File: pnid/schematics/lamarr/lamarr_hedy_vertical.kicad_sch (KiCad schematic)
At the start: 102 parts, among them U1 Rocket_Big

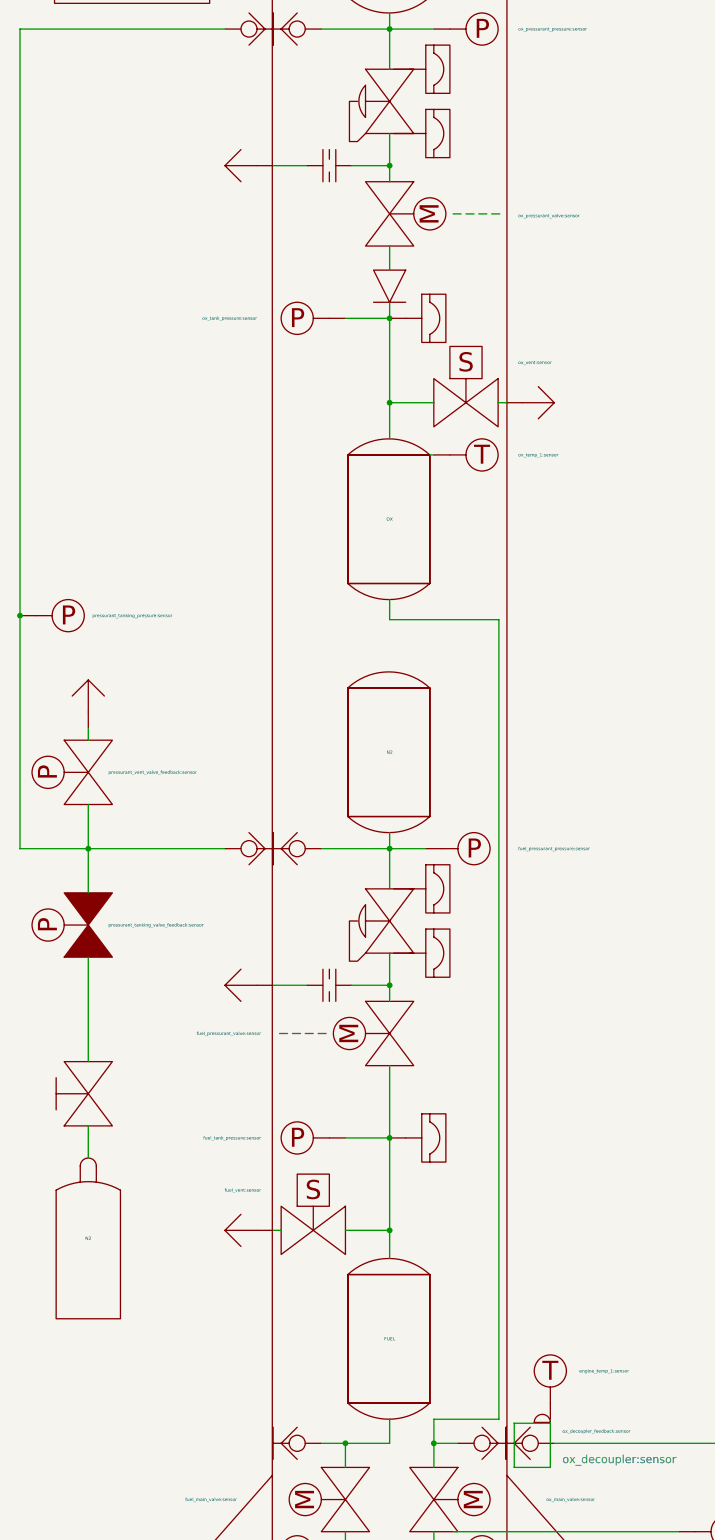
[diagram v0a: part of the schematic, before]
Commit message: Added fuel/ox pressurant vent to the pnid & mapping Added servo controlled throttle to the pnid & mapping
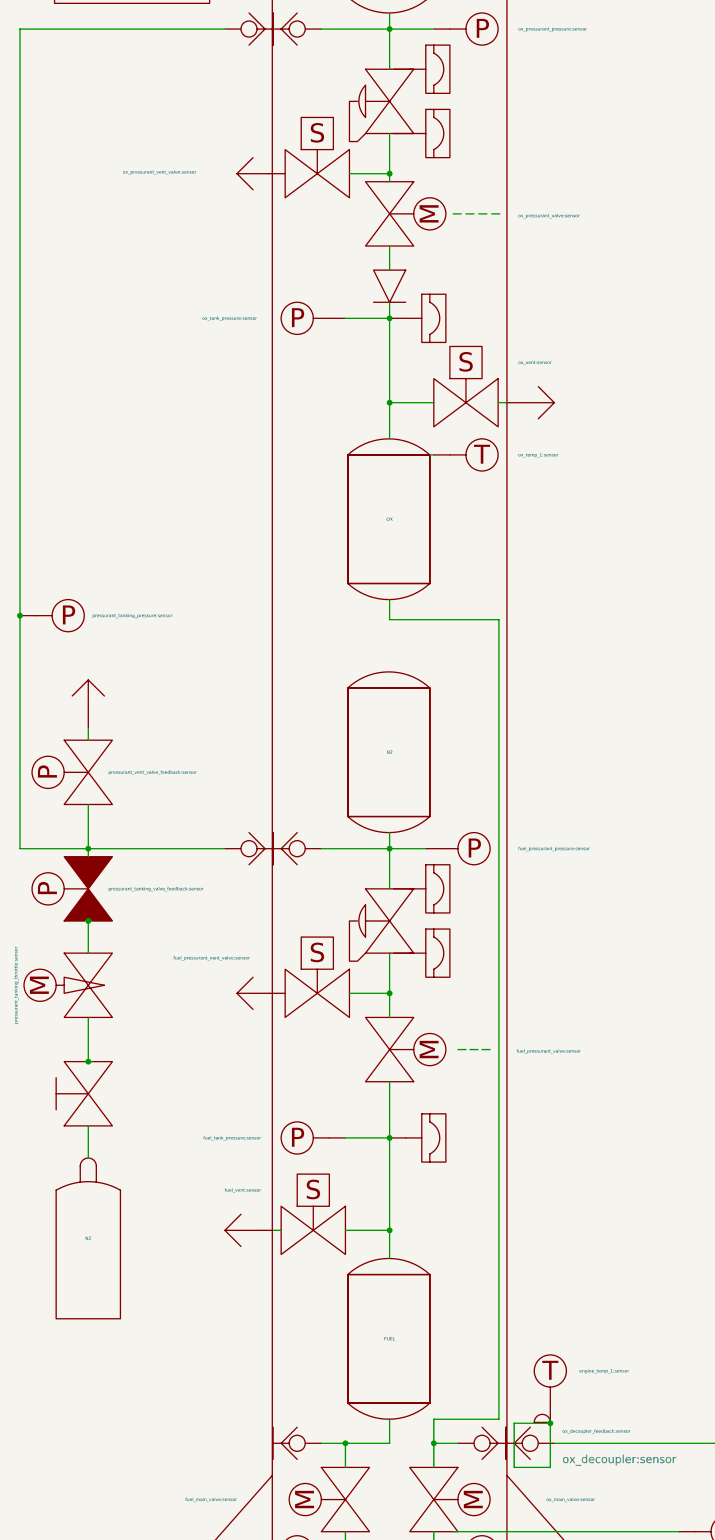
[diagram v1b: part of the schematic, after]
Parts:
- removed Orifice1, Orifice2: Orifice, symbol PnID-Lib:Orifice
- added fuel_pressurant_vent_valve: fuel_pressurant_vent_valve:sensor, symbol PnID-Lib:Valve_Solenoid_NO
- added ox_pressurant_vent_valve: ox_pressurant_vent_valve:sensor, symbol PnID-Lib:Valve_Solenoid_NO
- added pressurant_tanking_throttle: pressurant_tanking_throttle:sensor, symbol PnID-Lib:Valve_Needle_Servo
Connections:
- net at engine.~ (C): now also venturi1.~
- net at ox_venturi.~: now also ox_main_valve.~, ox_venturi_pressure.~; no longer engine.~ (C)
- net at venturi1.~: now also fuel_main_valve.~, fuel_venturi_pressure.~; no longer engine.~ (C)
- net at dewar_needle_valve?.~: now also C2.~, C3.~, press_in.~; no longer C1.~
- net at pressurant_tanking_valve_(A1).~: now also pressurant_tanking_throttle.~; no longer dewar_manual_valve1.~
- net at ox_pressurant_valve.~, pressurantPressureRegulator2.~: now also ox_pressurant_vent_valve.~
- net at fuel_pressurant_valve.~, pressurantPressureRegulator1.~: now also fuel_pressurant_vent_valve.~
- net at Vent5.~: now also fuel_pressurant_vent_valve.~
- net at Vent4.~: now also ox_pressurant_vent_valve.~
- new net: engine.~ (C), ox_venturi.~
- new net: OX.~, ox_main_valve.~, ox_quick_connect.~
- new net: DewarOverPressureValve?.~, LOX.~, dewar_pressurize_solenoid.~
- new net: C1.~, dewar_needle_valve?.~
- new net: dewar_manual_valve1.~, pressurant_tanking_throttle.~
- new net: FUEL.~, fuel_main_valve.~, ox_quick_connect1.~

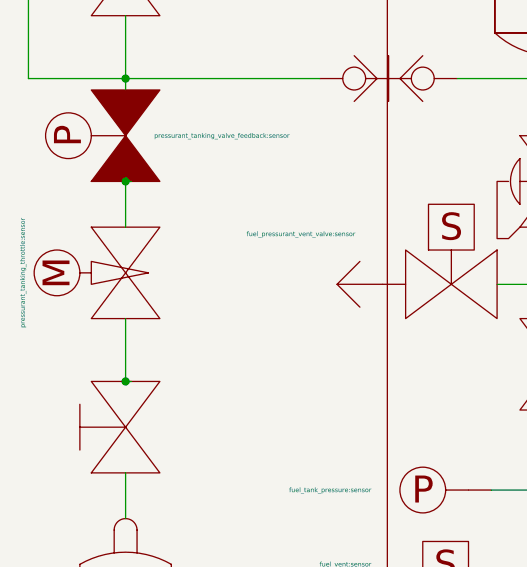
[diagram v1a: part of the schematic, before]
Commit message: Static fire 25.8.2025 setup. Changes were not reviewd by me (raffael rott)
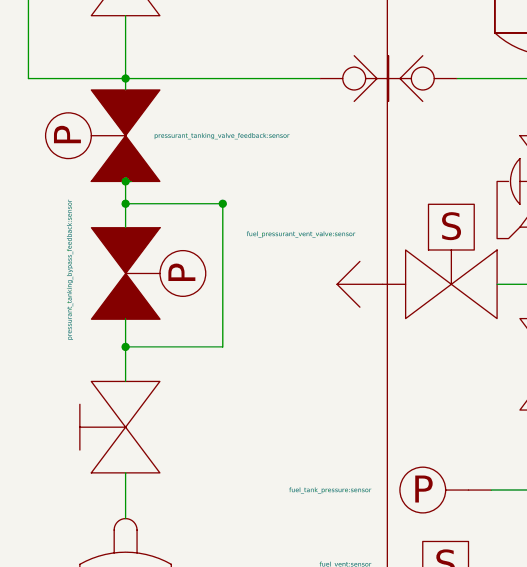
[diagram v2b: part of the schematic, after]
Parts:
- removed pressurant_tanking_throttle: pressurant_tanking_throttle:sensor, symbol PnID-Lib:Valve_Needle_Servo
- added pressurant_tanking_bypass: pressurant_tanking_bypass_feedback:sensor, symbol PnID-Lib:Valve_Pneumatic
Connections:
- net at engine.~ (C): now also venturi1.~
- net at ox_venturi.~: now also ox_main_valve.~, ox_venturi_pressure.~; no longer engine.~ (C)
- net at venturi1.~: now also fuel_main_valve.~, fuel_venturi_pressure.~; no longer engine.~ (C)
- net at dewar_needle_valve?.~: now also C2.~, C3.~, press_in.~; no longer C1.~
- net at pressurant_tanking_valve_(A1).~: now also dewar_manual_valve1.~
- net at dewar_manual_valve1.~: now also N2.~
- new net: engine.~ (C), ox_venturi.~
- new net: OX.~, ox_main_valve.~, ox_quick_connect.~
- new net: DewarOverPressureValve?.~, LOX.~, dewar_pressurize_solenoid.~
- new net: C1.~, dewar_needle_valve?.~
- new net: ox_pressurant_valve.~, ox_pressurant_vent_valve.~, pressurantPressureRegulator2.~
- new net: FUEL.~, fuel_main_valve.~, ox_quick_connect1.~
- new net: fuel_pressurant_valve.~, fuel_pressurant_vent_valve.~, pressurantPressureRegulator1.~
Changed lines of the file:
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@@
 	)
 	(junction
-		(at 19.685 73.025)
+		(at 19.685 53.2789)
 		(diameter 0)
 		(color 0 0 0 0)
@@
 	)
 	(junction
+		(at 30.48 53.2789)
+		(diameter 0)
+		(color 0 0 0 0)
+	)
+	(junction
 		(at 67.31 -90.17)
 		(diameter 0)
 		(color 0 0 0 0)
 	)
+	(junction
+		(at 19.685 69.1876)
+		(diameter 0)
+		(color 0 0 0 0)
+	)
 	(wire
 		(pts
@@
 	(wire
 		(pts
+			(xy 30.48 53.2789) (xy 30.48 69.1876)
+		)
+		(stroke
+			(width 0)
+			(type default)
+		)
+	)
+	(wire
+		(pts
 			(xy 60.325 164.846) (xy 64.77 164.846)
 		)
@@
 	(wire
 		(pts
-			(xy 19.685 50.8) (xy 19.685 55.88)
+			(xy 19.685 50.8) (xy 19.685 53.2789)
 		)
 		(stroke
@@
 	(wire
 		(pts
+			(xy 19.685 53.2789) (xy 30.48 53.2789)
+		)
+		(stroke
+			(width 0)
+			(type default)
+		)
+	)
+	(wire
+		(pts
 			(xy 73.025 39.37) (xy 67.31 39.37)
 		)
@@
 	(wire
 		(pts
+			(xy 19.685 69.1876) (xy 19.685 73.025)
+		)
+		(stroke
+			(width 0)
+			(type default)
+		)
+	)
+	(wire
+		(pts
 			(xy 69.85 164.846) (xy 74.295 164.846)
 		)
@@
 	(wire
 		(pts
+			(xy 30.48 69.1876) (xy 19.685 69.1876)
+		)
+		(stroke
+			(width 0)
+			(type default)
+		)
+	)
+	(wire
+		(pts
 			(xy 67.31 -92.71) (xy 67.31 -90.17)
 		)
@@
 	(wire
 		(pts
+			(xy 30.48 53.2789) (xy 30.7334 53.2789)
+		)
+		(stroke
+			(width 0)
+			(type default)
+		)
+	)
+	(wire
+		(pts
 			(xy 92.71 130.175) (xy 92.71 137.16)
 		)
@@
 	(wire
 		(pts
+			(xy 19.685 53.2789) (xy 19.685 55.88)
+		)
+		(stroke
+			(width 0)
+			(type default)
+		)
+	)
+	(wire
+		(pts
 			(xy 8.89 39.37) (xy 19.685 39.37)
 		)
@@
 	(wire
 		(pts
-			(xy 19.685 66.04) (xy 19.685 73.025)
+			(xy 19.685 66.04) (xy 19.685 69.1876)
 		)
 		(stroke
@@
 	(wire
 		(pts
-			(xy 20.32 73.025) (xy 19.685 73.025)
-		)
-		(stroke
-			(width 0)
-			(type default)
-		)
-	)
-	(wire
-		(pts
 			(xy 146.685 59.69) (xy 147.955 59.69)
 		)
@@
 	)
 	(symbol
-		(lib_id "PnID-Lib:Valve_Needle_Servo")
-		(at 19.685 60.96 90)
-		(unit 1)
-		(exclude_from_sim no)
-		(in_bom yes)
-		(on_board yes)
-		(dnp no)
-		(fields_autoplaced yes)
-		(property "Reference" "pressurant_tanking_throttle"
-			(at 6.985 60.96 0)
-			(effects
-				(font
-					(size 0.508 0.508)
-				)
-				(hide yes)
-			)
-		)
-		(property "Value" "pressurant_tanking_throttle:sensor"
-			(at 8.255 60.96 0)
-			(effects
-				(font
-					(size 0.508 0.508)
-				)
-			)
-		)
-		(property "Footprint" ""
-			(at 19.685 60.96 0)
-			(effects
-				(font
-					(size 0.508 0.508)
-				)
-				(hide yes)
-			)
-		)
-		(property "Datasheet" ""
-			(at 19.685 60.96 0)
-			(effects
-				(font
-					(size 0.508 0.508)
-				)
-				(hide yes)
-			)
-		)
-		(property "Description" ""
-			(at 19.685 60.96 0)
-			(effects
-				(font
-					(size 1.27 1.27)
-				)
-				(hide yes)
-			)
-		)
-		(property "Action_Reference" " "
-			(at 19.685 60.96 0)
-			(effects
-				(font
-					(size 1.27 1.27)
-				)
-				(hide yes)
-			)
-		)
-		(pin "~"
-		)
-		(pin "~"
-		)
-		(instances
-			(project ""
-				(path "/604fc9f3-63a6-4133-afd1-4a5c2507dc1d"
-					(reference "pressurant_tanking_throttle")
-					(unit 1)
-				)
-			)
-		)
-	)
-	(symbol
 		(lib_id "PnID-Lib:Motor")
 		(at 94.615 -132.715 0)
@@
 					(unit 1)
 				)
+			)
+		)
+	)
+	(symbol
+		(lib_name "Valve_Pneumatic_3")
+		(lib_id "PnID-Lib:Valve_Pneumatic")
+		(at 19.6994 61.0275 270)
+		(mirror x)
+		(unit 1)
+		(exclude_from_sim no)
+		(in_bom yes)
+		(on_board yes)
+		(dnp no)
+		(property "Reference" "pressurant_tanking_bypass"
+			(at 30.9516 61.0275 0)
+			(effects
+				(font
+					(size 0.508 0.508)
+				)
+				(hide yes)
+			)
+		)
+		(property "Value" "pressurant_tanking_bypass_feedback:sensor"
+			(at 13.462 52.832 0)
+			(effects
+				(font
+					(size 0.508 0.508)
+				)
+				(justify right)
+			)
+		)
+		(property "Footprint" ""
+			(at 19.6994 61.0275 0)
+			(effects
+				(font
+					(size 0.508 0.508)
+				)
+				(hide yes)
+			)
+		)
+		(property "Datasheet" ""
+			(at 19.6994 61.0275 0)
+			(effects
+				(font
+					(size 0.508 0.508)
+				)
+				(hide yes)
+			)
+		)
+		(property "Description" ""
+			(at 19.6994 61.0275 0)
+			(effects
+				(font
+					(size 1.27 1.27)
+				)
+				(hide yes)
+			)
+		)
+		(property "Unit" "%"
+			(at 19.6994 61.0275 0)
+			(effects
+				(font
+					(size 0.508 0.508)
+				)
+				(hide yes)
+			)
+		)
+		(property "Action_Reference" " "
+			(at 19.6994 61.0275 0)
+			(effects
+				(font
+					(size 1.27 1.27)
+				)
+				(hide yes)
+			)
+		)
+		(pin "~"
+		)
+		(pin "~"
+		)
+		(instances
+			(project "lamarr_hedy_vertical"
+				(path "/604fc9f3-63a6-4133-afd1-4a5c2507dc1d"
+					(reference "pressurant_tanking_bypass")
+					(unit 1)
+				)

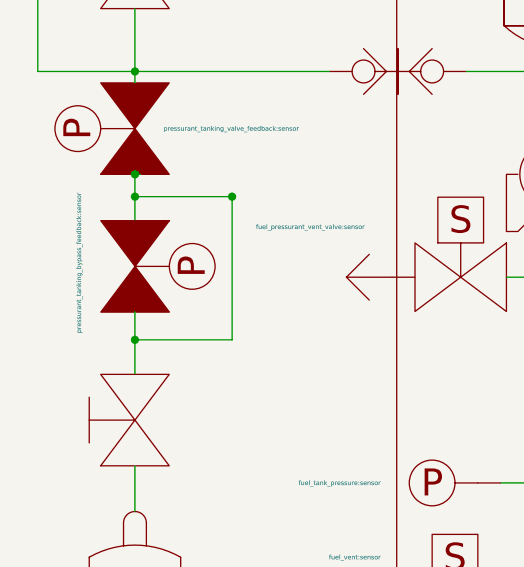
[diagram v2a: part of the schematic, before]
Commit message: added bypass solenoid to PnID
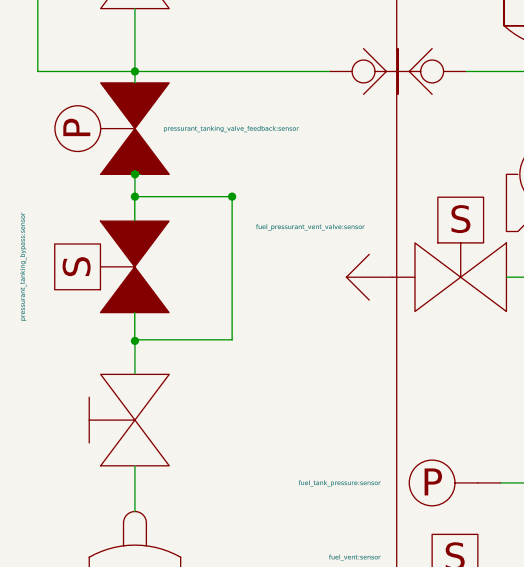
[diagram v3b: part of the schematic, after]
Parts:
- removed pressurant_tanking_bypass: pressurant_tanking_bypass_feedback:sensor, symbol PnID-Lib:Valve_Pneumatic
- added pressurant_tanking_bypass: pressurant_tanking_bypass:sensor, symbol PnID-Lib:Valve_Solenoid_NC
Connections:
- net at engine.~ (C): now also venturi1.~
- net at ox_venturi.~: now also ox_main_valve.~, ox_venturi_pressure.~; no longer engine.~ (C)
- net at venturi1.~: now also fuel_main_valve.~, fuel_venturi_pressure.~; no longer engine.~ (C)
- net at dewar_needle_valve?.~: now also C2.~, C3.~, press_in.~; no longer C1.~
- net at dewar_manual_valve1.~, pressurant_tanking_valve_(A1).~: now also pressurant_tanking_bypass.~
- new net: engine.~ (C), ox_venturi.~
- new net: OX.~, ox_main_valve.~, ox_quick_connect.~
- new net: DewarOverPressureValve?.~, LOX.~, dewar_pressurize_solenoid.~
- new net: C1.~, dewar_needle_valve?.~
- new net: ox_pressurant_valve.~, ox_pressurant_vent_valve.~, pressurantPressureRegulator2.~
- new net: FUEL.~, fuel_main_valve.~, ox_quick_connect1.~
- new net: fuel_pressurant_valve.~, fuel_pressurant_vent_valve.~, pressurantPressureRegulator1.~
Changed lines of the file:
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@@
 	)
 	(junction
-		(at 19.685 53.2789)
-		(diameter 0)
-		(color 0 0 0 0)
-	)
-	(junction
 		(at 179.07 70.485)
 		(diameter 0)
@@
 	)
 	(junction
+		(at 19.685 69.3068)
+		(diameter 0)
+		(color 0 0 0 0)
+	)
+	(junction
 		(at 179.07 59.69)
 		(diameter 0)
@@
 	)
 	(junction
+		(at 19.685 53.2789)
+		(diameter 0)
+		(color 0 0 0 0)
+	)
+	(junction
 		(at 67.31 62.23)
 		(diameter 0)
@@
 		(color 0 0 0 0)
 	)
-	(junction
-		(at 19.685 69.1876)
-		(diameter 0)
-		(color 0 0 0 0)
-	)
 	(wire
 		(pts
@@
 	(wire
 		(pts
+			(xy 19.6616 69.3068) (xy 19.685 69.3068)
+		)
+		(stroke
+			(width 0)
+			(type default)
+		)
+	)
+	(wire
+		(pts
 			(xy 148.59 59.69) (xy 150.495 59.69)
 		)
@@
 	(wire
 		(pts
+			(xy 19.6616 53.2789) (xy 19.6616 55.9992)
+		)
+		(stroke
+			(width 0)
+			(type default)
+		)
+	)
+	(wire
+		(pts
 			(xy 69.088 179.832) (xy 73.66 179.832)
 		)
@@
 	(wire
 		(pts
+			(xy 19.6616 53.2789) (xy 19.685 53.2789)
+		)
+		(stroke
+			(width 0)
+			(type default)
+		)
+	)
+	(wire
+		(pts
 			(xy 212.725 70.485) (xy 212.725 75.565)
 		)
@@
 	(wire
 		(pts
-			(xy 19.685 69.1876) (xy 19.685 73.025)
+			(xy 19.685 69.1876) (xy 19.685 69.3068)
 		)
 		(stroke
@@
 	(wire
 		(pts
+			(xy 19.685 69.3068) (xy 19.685 73.025)
+		)
+		(stroke
+			(width 0)
+			(type default)
+		)
+	)
+	(wire
+		(pts
 			(xy 30.48 53.2789) (xy 30.7334 53.2789)
 		)
@@
 	(wire
 		(pts
-			(xy 19.685 53.2789) (xy 19.685 55.88)
-		)
-		(stroke
-			(width 0)
-			(type default)
-		)
-	)
-	(wire
-		(pts
 			(xy 8.89 39.37) (xy 19.685 39.37)
 		)
@@
 	(wire
 		(pts
-			(xy 19.685 66.04) (xy 19.685 69.1876)
+			(xy 19.6616 66.1592) (xy 19.6616 69.3068)
 		)
 		(stroke
@@
 	)
 	(symbol
-		(lib_name "Valve_Pneumatic_3")
-		(lib_id "PnID-Lib:Valve_Pneumatic")
-		(at 19.6994 61.0275 270)
-		(mirror x)
-		(unit 1)
-		(exclude_from_sim no)
-		(in_bom yes)
-		(on_board yes)
-		(dnp no)
-		(property "Reference" "pressurant_tanking_bypass"
-			(at 30.9516 61.0275 0)
-			(effects
-				(font
-					(size 0.508 0.508)
-				)
-				(hide yes)
-			)
-		)
-		(property "Value" "pressurant_tanking_bypass_feedback:sensor"
-			(at 13.462 52.832 0)
-			(effects
-				(font
-					(size 0.508 0.508)
-				)
-				(justify right)
-			)
-		)
-		(property "Footprint" ""
-			(at 19.6994 61.0275 0)
-			(effects
-				(font
-					(size 0.508 0.508)
-				)
-				(hide yes)
-			)
-		)
-		(property "Datasheet" ""
-			(at 19.6994 61.0275 0)
-			(effects
-				(font
-					(size 0.508 0.508)
-				)
-				(hide yes)
-			)
-		)
-		(property "Description" ""
-			(at 19.6994 61.0275 0)
-			(effects
-				(font
-					(size 1.27 1.27)
-				)
-				(hide yes)
-			)
-		)
-		(property "Unit" "%"
-			(at 19.6994 61.0275 0)
-			(effects
-				(font
-					(size 0.508 0.508)
-				)
-				(hide yes)
-			)
-		)
-		(property "Action_Reference" " "
-			(at 19.6994 61.0275 0)
-			(effects
-				(font
-					(size 1.27 1.27)
-				)
-				(hide yes)
-			)
-		)
-		(pin "~"
-		)
-		(pin "~"
-		)
-		(instances
-			(project "lamarr_hedy_vertical"
-				(path "/604fc9f3-63a6-4133-afd1-4a5c2507dc1d"
-					(reference "pressurant_tanking_bypass")
-					(unit 1)
-				)
-			)
-		)
-	)
-	(symbol
 		(lib_id "PnID-Lib:Vent")
 		(at 19.685 12.7 270)
@@
 					(unit 1)
 				)
+			)
+		)
+	)
+	(symbol
+		(lib_name "Valve_Solenoid_NC_1")
+		(lib_id "PnID-Lib:Valve_Solenoid_NC")
+		(at 19.6616 61.0792 90)
+		(unit 1)
+		(exclude_from_sim no)
+		(in_bom yes)
+		(on_board yes)
+		(dnp no)
+		(property "Reference" "pressurant_tanking_bypass"
+			(at 8.4094 61.0792 0)
+			(effects
+				(font
+					(size 0.508 0.508)
+				)
+				(hide yes)
+			)
+		)
+		(property "Value" "pressurant_tanking_bypass:sensor"
+			(at 7.2156 61.0792 0)
+			(effects
+				(font
+					(size 0.508 0.508)
+				)
+			)
+		)
+		(property "Footprint" ""
+			(at 19.6616 61.0792 0)
+			(effects
+				(font
+					(size 0.508 0.508)
+				)
+				(hide yes)
+			)
+		)
+		(property "Datasheet" ""
+			(at 19.6616 61.0792 0)
+			(effects
+				(font
+					(size 0.508 0.508)
+				)
+				(hide yes)
+			)
+		)
+		(property "Description" ""
+			(at 19.6616 61.0792 0)
+			(effects
+				(font
+					(size 1.27 1.27)
+				)
+				(hide yes)
+			)
+		)
+		(property "Unit" "%"
+			(at 19.6616 61.0792 0)
+			(effects
+				(font
+					(size 0.508 0.508)
+				)
+				(hide yes)
+			)
+		)
+		(property "Action_Reference" " "
+			(at 19.6616 61.0792 0)
+			(effects
+				(font
+					(size 1.27 1.27)
+				)
+				(hide yes)
+			)
+		)
+		(pin "~"
+		)
+		(pin "~"
+		)
+		(instances
+			(project "lamarr_hedy_vertical"
+				(path "/604fc9f3-63a6-4133-afd1-4a5c2507dc1d"
+					(reference "pressurant_tanking_bypass")
+					(unit 1)
+				)
